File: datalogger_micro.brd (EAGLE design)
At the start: 38.1 x 40.6 mm, 30 parts, among them IC1 DS3231/SO, IC2 MEGA8-P, Q1 8/16/20MHz, U2 MIC5205

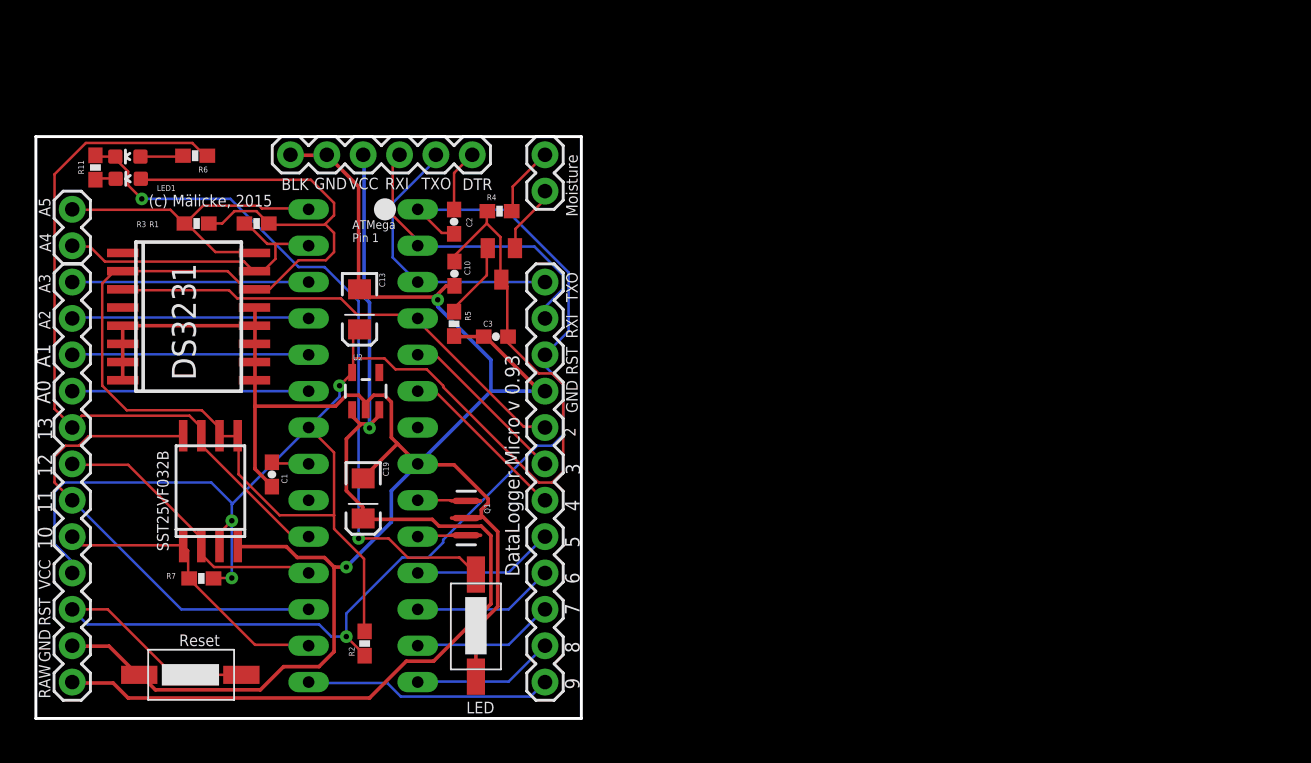
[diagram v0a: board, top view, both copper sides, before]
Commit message: version 0.94
first draft of 0.94, not the printed one.
integrates the LD117 voltage regulator
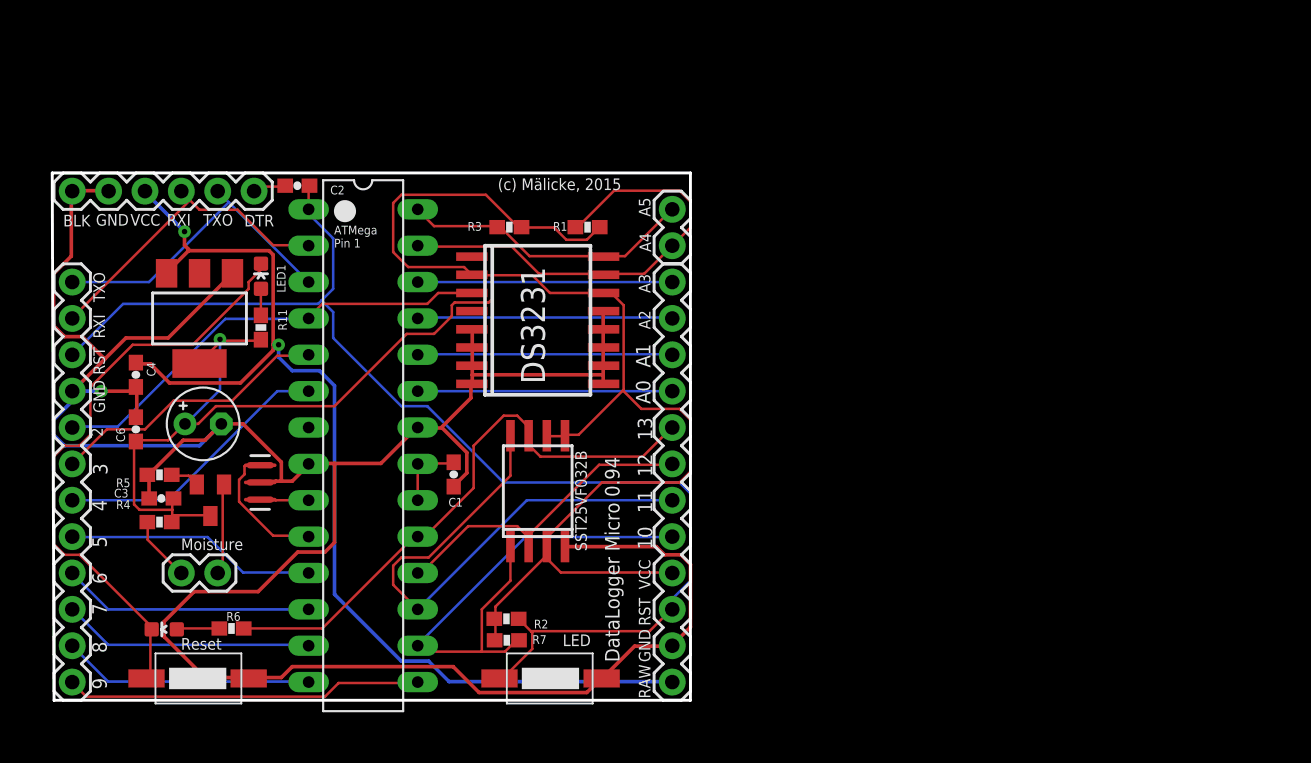
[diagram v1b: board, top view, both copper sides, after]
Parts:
- removed C10: 0.1uF, SparkFun:0603-CAP
- removed C13, C19: 10uF, SparkFun:EIA3216
- removed U2: MIC5205, SparkFun:SOT23-5
- added C4, C6: 0.1uF, SparkFun:0603-CAP
- added C5: 10uF, rcl:E2,5-5
- added IC3: LD117AS33TR, v-reg:SOT223
- moved JP2 41.9 mm to (44.5, 33.0)
- moved JP6 41.9 mm to (44.5, 2.54)
- moved JP4 35.1 mm to (12.7, 10.2), turned to 180 degrees
- moved D3 33.1 mm to (8.97, 6.22)
- moved R6 33.1 mm to (13.7, 6.28)
- moved JP7 33.0 mm to (2.54, 2.54)
- moved R4 32.2 mm to (8.64, 13.7), turned to 180 degrees
- moved Q2 26.2 mm to (12.2, 15.2)
- moved C3 26.0 mm to (8.76, 15.4)
- moved U$1 25.1 mm to (35.9, 2.79), turned to 180 degrees
- moved IC1 24.4 mm to (35.1, 27.8)
- moved R5 23.1 mm to (8.64, 17.0), turned to 180 degrees
- moved R1 23.1 mm to (38.5, 34.3)
- moved U$2 22.9 mm to (35.1, 15.9)
- moved R3 21.8 mm to (33.1, 34.3)
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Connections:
- removed net N$3: IC2.20
- net AREF: now also IC2.20
- net GND: now also C4.2, C5.-, C6.2, IC2.22, IC3.1; no longer C10.2, C13.C, C19.C, U2.2
- net GNDA: now also LED1.C; no longer R11.1
- net N$4: now also LED1.A, R11.1; no longer LED1.C, R11.2
- net RAW: now also C4.1, IC3.3; no longer C19.A, U2.1, U2.3
- net VCC: now also C5.+, C6.1, IC3.4, R11.2; no longer C10.1, C13.A, IC2.22, LED1.A, U2.5
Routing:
- net VCC: track 177.4 -> 145.6 mm, vias 3 -> 1
- net GND: track 158.2 -> 186.8 mm, vias 2 -> 1
- net D10: track 20.9 -> 36.7 mm
- net A4: track 21.5 -> 32.5 mm
- net SCK: track 51.3 -> 40.6 mm
- net D9: track 17.4 -> 25.0 mm
- net D3: track 12.0 -> 19.7 mm
- net D7: track 9.94 -> 17.6 mm
- net D5: track 9.93 -> 17.6 mm
- net D8: track 9.93 -> 17.6 mm
- net D6: track 9.94 -> 17.6 mm
- net D4: track 12.0 -> 19.7 mm
- net GNDA: track 49.1 -> 41.7 mm, vias 2 -> 0
- net N$2: track 2.39 -> 8.65 mm
- net MOSI: track 32.8 -> 38.3 mm
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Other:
- board size 38.1 x 40.6 mm -> 44.6 x 36.8 mm
- board text added: "DataLogger Micro 0.94"
- board text removed: "DataLogger Micro v 0.93"

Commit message: schematic rework for 0.95
Schematic rework for 0.95 version. Not productive, no layout.
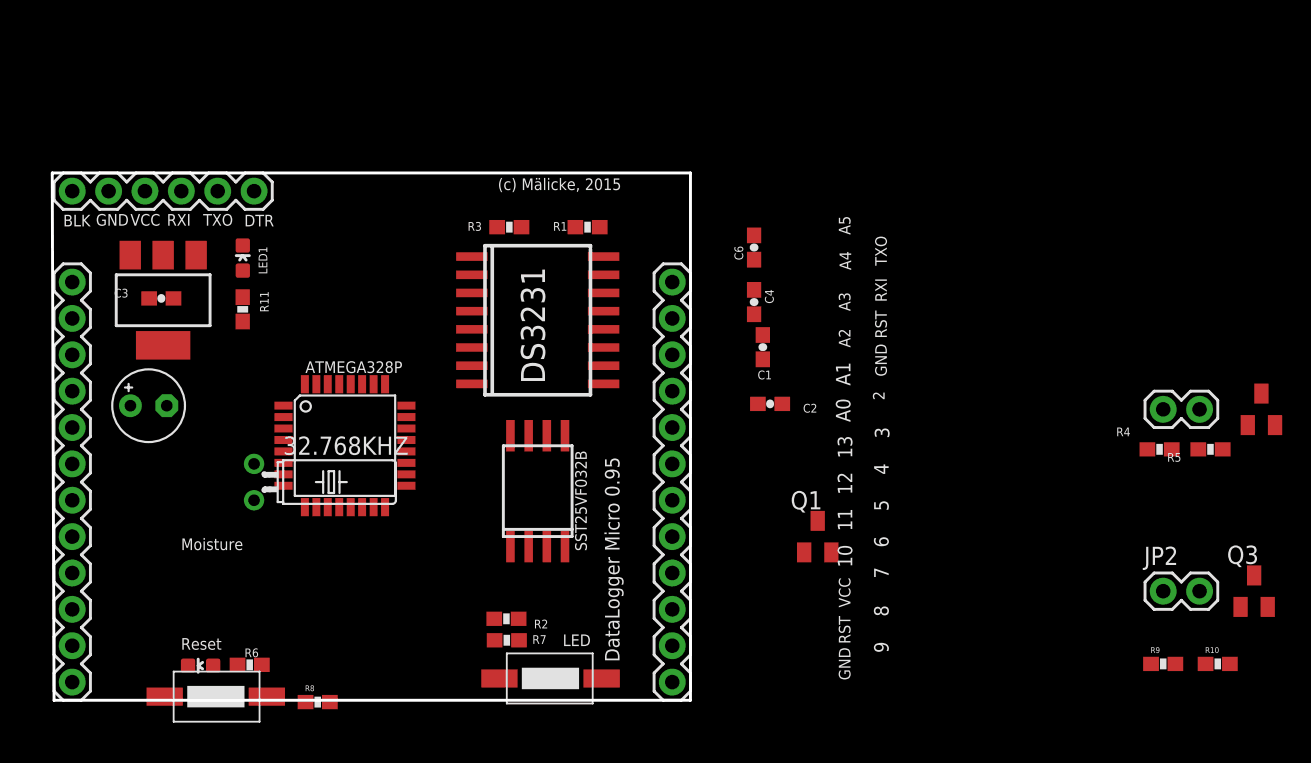
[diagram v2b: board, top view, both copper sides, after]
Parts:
- removed IC2: MEGA8-P, atmel:DIL28-3
- added 32.768KHZ: (no value), crystal:TC38H
- added ATMEGA328P: MEGA8-AI, atmel:TQFP32-08
- added Q3: (no value), semicon-smd-ipc:SOT23
- added R10, R9: 100, SparkFun:0603-RES
- added R8: 10k, SparkFun:0603-RES
- JP2: value (none) -> PAT
- Q1: value 8/16/20MHz -> (none); device Testing:RESONATOR-SMD-1:1 -> semicon-smd-ipc:SOT23
- moved Q2 73.7 mm to (85.6, 21.6), turned to 0 degrees
- moved R5 73.4 mm to (82.0, 18.8)
- moved R4 70.0 mm to (78.5, 18.8)
- moved JP4 69.5 mm to (81.3, 21.6)
- moved C6 45.0 mm to (50.2, 32.9)
- moved C4 43.5 mm to (50.2, 29.1)
- moved JP2 41.9 mm to (78.7, 8.89), turned to 0 degrees
- moved Q1 39.1 mm to (54.6, 12.7), turned to 0 degrees
- moved C2 36.4 mm to (51.3, 22.0)
- moved C1 23.3 mm to (50.8, 25.9)
- moved C3 14.0 mm to (8.76, 29.3)
- moved C5 4.02 mm to (7.87, 21.8)
- moved D3 3.59 mm to (11.5, 3.68)
- moved R6 2.84 mm to (14.9, 3.74)
- moved IC3 2.84 mm to (8.89, 29.2)
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- renumbered JP6 to JP3
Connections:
- removed net 3.3V: IC2.7
- removed net AREF: C1.2, IC2.20, IC2.21
- removed net RAW: C4.1, IC3.3, JP1.4, JP3.1
- removed net VCC: C3.2, C5.+, C6.1, IC1.14, IC1.2, IC3.4, JP3.4, Q2.3, R1.2, R11.2, R2.2, R3.2, R4.1, R7.1, U$2.3, U$2.5, U$2.6
- new net N$3: 32.768KHZ.2, ATMEGA328P.8
- new net N$5: JP2.1, Q3.1
- new net N$8: JP2.2, R9.2
- new net VCC-ST: ATMEGA328P.18, ATMEGA328P.20, C3.2, C5.+, IC3.4, JP3.2, Q2.3, Q3.3, R1.2, R11.2, R2.2, R3.2, R4.1, R7.1, R9.1, U$2.3, U$2.5, U$2.6
- new net VCC/2: ATMEGA328P.4, ATMEGA328P.6, C1.2, C6.1, IC1.14, IC1.2, JP1.4, Q1.3
- net A0: now also ATMEGA328P.23, JP3.7; no longer IC2.23, JP3.9
- net A1: now also ATMEGA328P.24, JP3.8, Q3.2, R10.1; no longer IC2.24, JP3.10
- net A2: now also ATMEGA328P.25, JP3.9; no longer IC2.25, JP3.11
- net A3: now also ATMEGA328P.26, JP3.10; no longer IC2.26, JP3.12
- net A4: now also ATMEGA328P.27, JP3.11; no longer IC2.27, JP2.1
- net A5: now also ATMEGA328P.28, JP3.12; no longer IC2.28, JP2.2
- net D10: now also ATMEGA328P.14, JP3.3; no longer IC2.16, JP3.5
- net D2: now also ATMEGA328P.32; no longer IC2.4
- net D3: now also ATMEGA328P.1; no longer IC2.5
- net D4: now also ATMEGA328P.2, R6.1; no longer IC2.6
- net D5: now also ATMEGA328P.9, Q1.1, R8.1; no longer IC2.11
- net D6: now also ATMEGA328P.10; no longer IC2.12
- net D7: now also ATMEGA328P.11; no longer IC2.13
- net D8: now also ATMEGA328P.12; no longer IC2.14
- net D9: now also ATMEGA328P.13; no longer IC2.15
- net GND: now also ATMEGA328P.21, ATMEGA328P.3, ATMEGA328P.5, R10.2, R8.2; no longer IC2.22, IC2.8, JP3.2, Q1.2
- net MISO: now also ATMEGA328P.16, JP3.5; no longer IC2.18, JP3.7
- net MOSI: now also ATMEGA328P.15, JP3.4; no longer IC2.17, JP3.6
- net N$1: now also C4.1, IC3.3, Q1.2; no longer IC2.9, Q1.1
- net N$2: now also 32.768KHZ.1, ATMEGA328P.7; no longer IC2.10, Q1.3
- net RESET: now also ATMEGA328P.29, JP3.1; no longer IC2.1, JP3.3
- net RXI: now also ATMEGA328P.30; no longer IC2.2
- net SCK: now also ATMEGA328P.17, JP3.6; no longer IC2.19, JP3.8, R6.1
- net TXO: now also ATMEGA328P.31; no longer IC2.3
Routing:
- net GND: track 186.8 -> 0.00 mm, vias 1 -> 0
- net VCC: track 145.6 -> 0.00 mm, vias 1 -> 0
- net RESET: track 85.3 -> 0.00 mm
- net RAW: track 78.1 -> 0.00 mm, vias 2 -> 0
- net GNDA: track 41.7 -> 0.00 mm
- net SCK: track 40.6 -> 0.00 mm
- net MOSI: track 38.3 -> 0.00 mm
- net D10: track 36.7 -> 0.00 mm
- net A4: track 32.5 -> 0.00 mm
- net D2: track 31.9 -> 0.00 mm
- net D9: track 25.0 -> 0.00 mm
- net RXI: track 23.0 -> 0.00 mm
- net MISO: track 23.0 -> 0.00 mm
- net TXO: track 22.2 -> 0.00 mm
- net A5: track 20.5 -> 0.00 mm
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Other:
- board text added: "DataLogger Micro 0.95"
- board text removed: "ATMega Pin 1"
- board text removed: "DataLogger Micro 0.94"
- board text removed: "RAW"

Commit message: layout rework
Still need to include the battery, maybe replace LM117
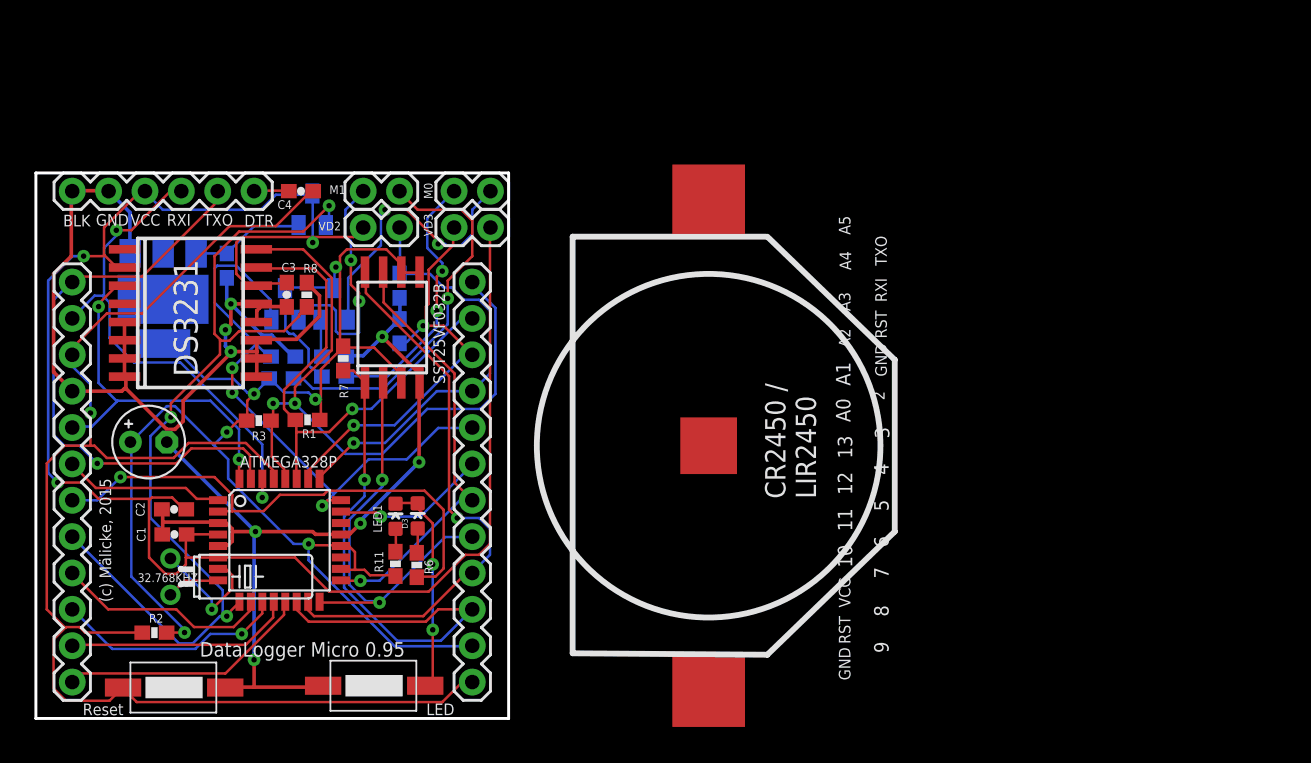
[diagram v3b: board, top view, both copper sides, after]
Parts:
- removed JP2, JP4: PAT, SparkFun:1X02
- added M0, M1, VD2, VD3: PAT, SparkFun:1X02
- added R12, R13: VAR, SparkFun:0603-RES
- added U$3: CR2450SMT, battery:CR2450SMT
- moved Q3 70.6 mm to (17.4, 29.0), flipped to the bottom
- moved R10 68.7 mm to (17.3, 25.3), flipped to the bottom, turned to 180 degrees
- moved Q2 65.2 mm to (20.8, 29.0), flipped to the bottom
- moved R9 64.7 mm to (17.1, 23.7), flipped to the bottom, turned to 180 degrees
- moved R5 61.6 mm to (20.8, 25.3), flipped to the bottom
- moved R4 57.9 mm to (20.8, 23.9), flipped to the bottom
- moved C1 43.1 mm to (9.68, 12.9), turned to 0 degrees
- moved C2 42.3 mm to (9.65, 14.6)
- moved Q1 42.1 mm to (19.3, 35.6), flipped to the bottom
- moved C6 36.9 mm to (13.3, 31.6), flipped to the bottom, turned to 270 degrees
- moved C4 32.6 mm to (18.5, 36.8), turned to 180 degrees
- moved R8 28.5 mm to (18.9, 29.6), turned to 90 degrees
- moved U$1 26.3 mm to (9.65, 2.16)
- moved R2 24.6 mm to (8.28, 5.99), turned to 0 degrees
- moved IC1 24.3 mm to (10.8, 28.3)
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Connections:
- net A2: now also R12.2, VD2.2
- net A3: now also R13.2, VD3.2
- net DTR: now also C4.2; no longer C2.2
- net GND: now also C2.2, R12.1, R13.1, U$3.P$2; no longer C4.2
- net N$1: now also C6.1; no longer C4.1
- net N$5: now also M1.1; no longer JP2.1
- net N$6: now also M0.1; no longer JP4.1
- net N$8: now also M1.2; no longer JP2.2
- net N$9: now also M0.2; no longer JP4.2
- net RESET: now also C4.1; no longer C2.1
- net VCC-ST: no longer C3.2
- net VCC/2: now also C2.1, C3.2, U$3.P$3, VD2.1, VD3.1; no longer C6.1
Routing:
- net GND: track 0.00 -> 139.9 mm, vias 0 -> 8
- net VCC/2: track 0.00 -> 126.1 mm, vias 0 -> 3
- net VCC-ST: track 0.00 -> 114.1 mm, vias 0 -> 6
- net RESET: track 0.00 -> 100.4 mm, vias 0 -> 1
- net D5: track 0.00 -> 63.5 mm, vias 0 -> 3
- net A5: track 0.00 -> 48.9 mm, vias 0 -> 2
- net A1: track 0.00 -> 42.6 mm, vias 0 -> 3
- net D10: track 0.00 -> 41.7 mm, vias 0 -> 1
- net TXO: track 0.00 -> 41.3 mm, vias 0 -> 1
- net MOSI: track 0.00 -> 39.6 mm, vias 0 -> 1
- net D4: track 0.00 -> 36.6 mm, vias 0 -> 1
- net A4: track 0.00 -> 36.3 mm, vias 0 -> 1
- net RXI: track 0.00 -> 35.4 mm, vias 0 -> 2
- net MISO: track 0.00 -> 30.4 mm, vias 0 -> 2
- net A2: track 0.00 -> 30.1 mm, vias 0 -> 1
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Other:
- board size 44.6 x 36.8 mm -> 33 x 38.1 mm
- board text removed: "Moisture"

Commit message: same as last
another variant of LIR2450
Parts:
- added G1: CR2450V, battery:CR2450V
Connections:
- net GND: now also G1.-
- net VCC/2: now also G1.+
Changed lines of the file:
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@@
 <element name="R13" library="SparkFun" package="0603-RES" value="VAR" x="25.4" y="27.051" rot="MR270"/>
 <element name="U$3" library="battery" package="CR2450SMT" value="CR2450SMT" x="46.99" y="19.05" rot="R90"/>
+<element name="G1" library="battery" package="CR2450V" value="CR2450V" x="66.04" y="17.78"/>
 </elements>
 <signals>
@@
 <via x="15.33525" y="13.04925" extent="1-16" drill="0.381"/>
 <contactref element="U$3" pad="P$2"/>
-<wire x1="13.227" y1="2.159" x2="46.99" y2="1.95" width="0" layer="19" extent="1-1"/>
+<contactref element="G1" pad="-"/>
+<wire x1="26.76525" y1="17.907" x2="46.99" y2="1.95" width="0" layer="19" extent="1-1"/>
+<wire x1="70.231" y1="17.78" x2="1.23825" y2="24.1935" width="0" layer="19" extent="1-1"/>
 </signal>
 <signal name="RESET">
@@
 <via x="1.524" y="16.47825" extent="1-16" drill="0.381"/>
 <contactref element="U$3" pad="P$3"/>
-<wire x1="9.04875" y1="10.0965" x2="46.99" y2="36.15" width="0" layer="19" extent="1-1"/>
+<contactref element="G1" pad="+"/>
+<wire x1="31.75" y1="34.29" x2="46.99" y2="36.15" width="0" layer="19" extent="1-1"/>
+<wire x1="63.5" y1="12.7" x2="0.85725" y2="17.145" width="0" layer="19" extent="16-16"/>
 </signal>
 <signal name="N$1">
